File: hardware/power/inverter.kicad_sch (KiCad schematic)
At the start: 25 parts, among them U301 TPS54560

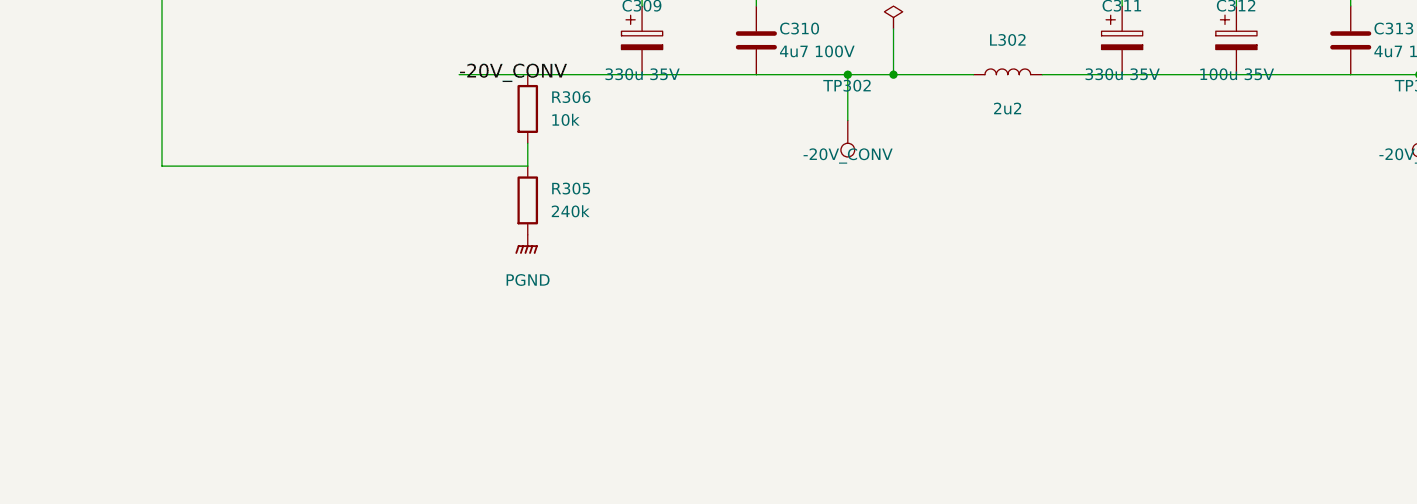
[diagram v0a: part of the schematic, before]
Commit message: Power board: confirm decision 100 values, add start-up ramp
The user confirmed the UVLO thresholds (21.1 / 18.7 V), the oscillator
(4.7 k / 560 p), the switch and LED at the rear edge and the L / F
part-number categories.

An averaged ngspice model (scripts/startup_sim.py) showed the fixed
2.6 ms soft-start into about 1.1 mF per rail takes 183-262 W from the
brick, over the GSM120B24's 126 W hiccup threshold. Each converter now
gets 47 nF from its output through a 1N4148W into FB (1 M and a clamp
diode reset the node): the rails rise with tau 11.3 ms and the input
peaks at about 54 W. Netlist checks 0 problems, ERC 0/0.

Co-Authored-By: Claude Opus 5.5 <noreply@anthropic.com>
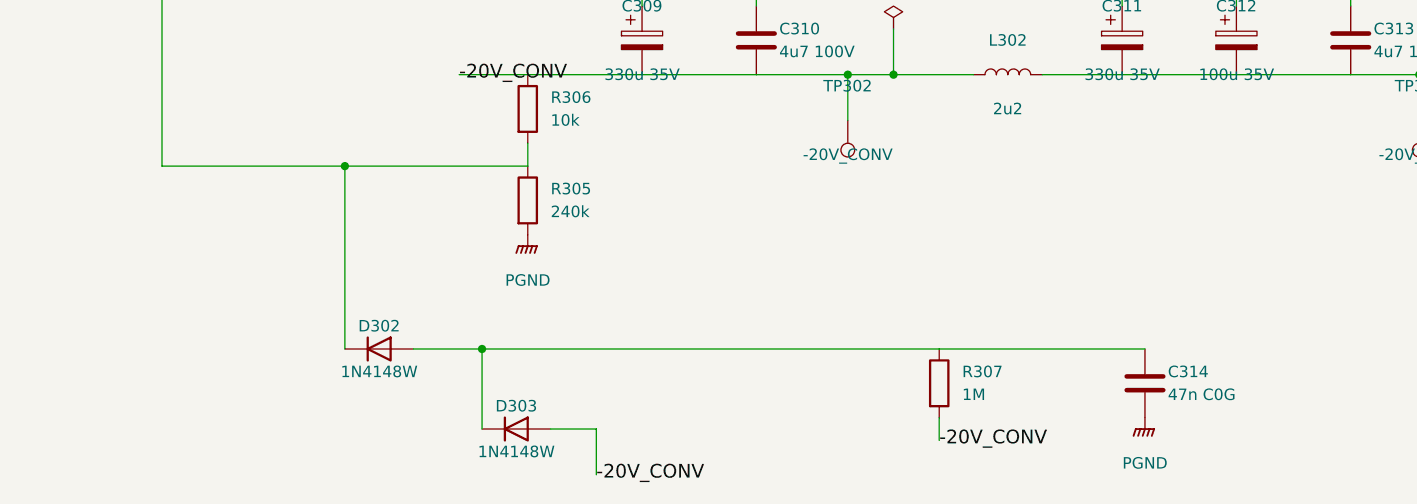
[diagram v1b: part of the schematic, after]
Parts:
- added C314: 47n C0G, Capacitor_SMD:C_0805_2012Metric, symbol Device:C
- added D302, D303: 1N4148W, Diode_SMD:D_SOD-123, symbol Device:D
- added R307: 1M, Resistor_SMD:R_0805_2012Metric, symbol Device:R
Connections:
- net -20V_CONV: now also D303.2 (A), R307.2
- net PGND: now also C314.2
- net at R305.1, R306.2, U301.5 (FB): now also D302.1 (K)
- new net: C314.1, D302.2 (A), D303.1 (K), R307.1

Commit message: Power board: E24 dividers, rear-panel rocker, last parts chosen (decisions 156-159)
- 156: UVLO 680k/39k (start 21.3 V, stop 19.0 V), RT 240k, buck
  compensation 16k; design.py and startup_sim.py rerun (start-up unchanged,
  GSM220B24 limit in the model)
- 157: power switch a Legion SS11-BBIWG-R20-R rocker on the rear panel,
  wired to J102 (JST XH 2-pin) in place of SW101; counted in costs.py
- 158: C103 Nichicon UHE1H101MPD radial; sync caps 10 pF C0G 50 V 0603
- 159: D201 SS54 on D_SMA to match LCSC C22452
- Netlist checks 0 problems, ERC 0/0; estimate 764/1045/1641 EUR
  (4/8/16 ch), 28 fee types

Co-Authored-By: Claude Opus 5.5 <noreply@anthropic.com>
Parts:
- C307: value 10p C0G 100V -> 10p C0G; footprint Capacitor_SMD:C_0805_2012Metric -> Capacitor_SMD:C_0603_1608Metric; MPN (none) -> CL10C100JB8NNNC; Manufacturer (none) -> Samsung Electro-Mechanics; ProjectPN SX-C-022 -> SX-C-029; Supplier (none) -> LCSC; SupplierPN (none) -> C1634
- R301: value 732k -> 680k; MPN (none) -> 0805W8F6803T5E; Manufacturer (none) -> UNI-ROYAL; ProjectPN SX-R-085 -> SX-R-036; Supplier (none) -> LCSC; SupplierPN (none) -> C17797
- R302: value 42k2 -> 39k; MPN (none) -> 0805W8F3902T5E; Manufacturer (none) -> UNI-ROYAL; ProjectPN SX-R-086 -> SX-R-104; Supplier (none) -> LCSC; SupplierPN (none) -> C25826
- R304: value 243k -> 240k; ProjectPN SX-R-083 -> SX-R-084

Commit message: Power board: PCB placed and routed by scripts, panel-mount brick jack, small module without chain 2 (decisions 182, 185, 186)
Co-Authored-By: Claude Opus 5.5 <noreply@anthropic.com>
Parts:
- L301: footprint (none) -> syntsamix:L_Bourns_SRP1265A; Note Footprint to draw from the maker's drawing at PCB layout -> (none)
- U301: footprint Package_SO:Texas_R-PDSO-G8_EP2.95x4.9mm_Mask2.4x3.1mm_ThermalVias -> Package_SO:Texas_R-PDSO-G8_EP2.95x4.9mm_Mask2.4x3.1mm
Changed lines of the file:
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@@
 			)
 		)
-		(property "Footprint" ""
+		(property "Footprint" "syntsamix:L_Bourns_SRP1265A"
 			(at 199.39 130.81 0)
 			(hide yes)
@@
 		)
 		(property "SupplierPN" "C2041465"
-			(at 199.39 130.81 0)
-			(hide yes)
-			(show_name no)
-			(do_not_autoplace no)
-			(effects
-				(font
-					(size 1.27 1.27)
-				)
-			)
-		)
-		(property "Note" "Footprint to draw from the maker's drawing at PCB layout"
 			(at 199.39 130.81 0)
 			(hide yes)
@@
 			)
 		)
-		(property "Footprint" "Package_SO:Texas_R-PDSO-G8_EP2.95x4.9mm_Mask2.4x3.1mm_ThermalVias"
+		(property "Footprint" "Package_SO:Texas_R-PDSO-G8_EP2.95x4.9mm_Mask2.4x3.1mm"
 			(at 152.4 127 0)
 			(hide yes)

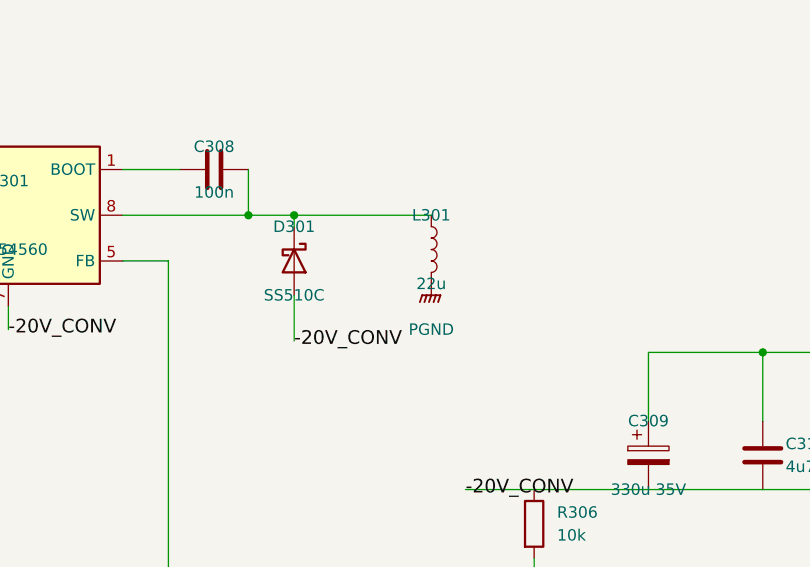
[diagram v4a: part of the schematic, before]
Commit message: Power board: DNP switch-node RC snubber footprints across D201 and D301, bench EMI checklist (decision 189)
R208/C215 (SW to PGND, above D201) and R308/C315 (SW to -20V_CONV, beside
D301), 0805, not fitted: values from a bench measurement of the ringing on the
first boards ("Bench, first boards" in CHECKLISTS.md, with the input filter
check of decision 187). placement.py takes DNP and BOM flags from the symbols.
ERC 0/0, DRC 0, parity clean; cost unchanged.

Co-Authored-By: Claude Opus 5.5 <noreply@anthropic.com>
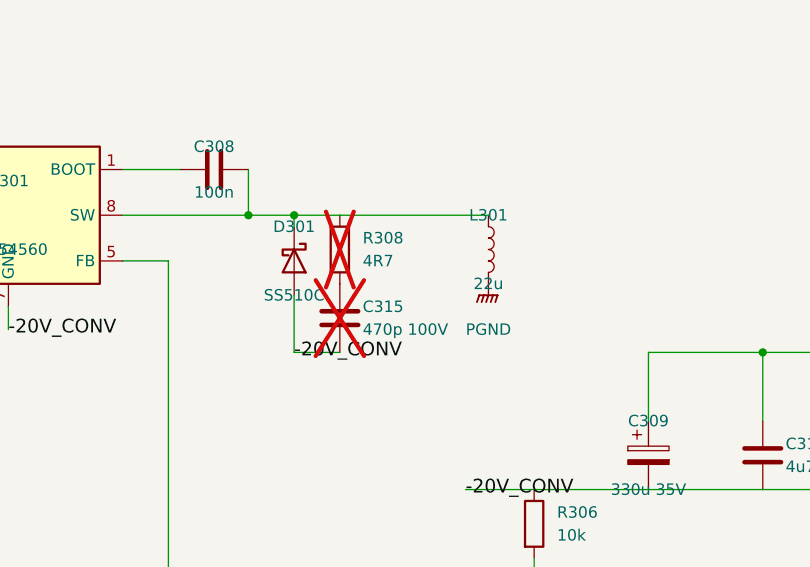
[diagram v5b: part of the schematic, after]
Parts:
- added C315: 470p 100V, Capacitor_SMD:C_0805_2012Metric, symbol Device:C
- added R308: 4R7, Resistor_SMD:R_0805_2012Metric, symbol Device:R
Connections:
- net -20V_CONV: now also C315.2
- net at C308.2, D301.1 (K), L301.1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: now also R308.1
- new net: C315.1, R308.2
